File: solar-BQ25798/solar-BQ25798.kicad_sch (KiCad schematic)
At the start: 83 parts, among them J101 Power In, J102 Power OUT, J103 Power OUT, Q101 DMP4013LFGQ-13, Q102 2N7002, U101 HT75xx-1-SOT89, U102 INA219AxDCN

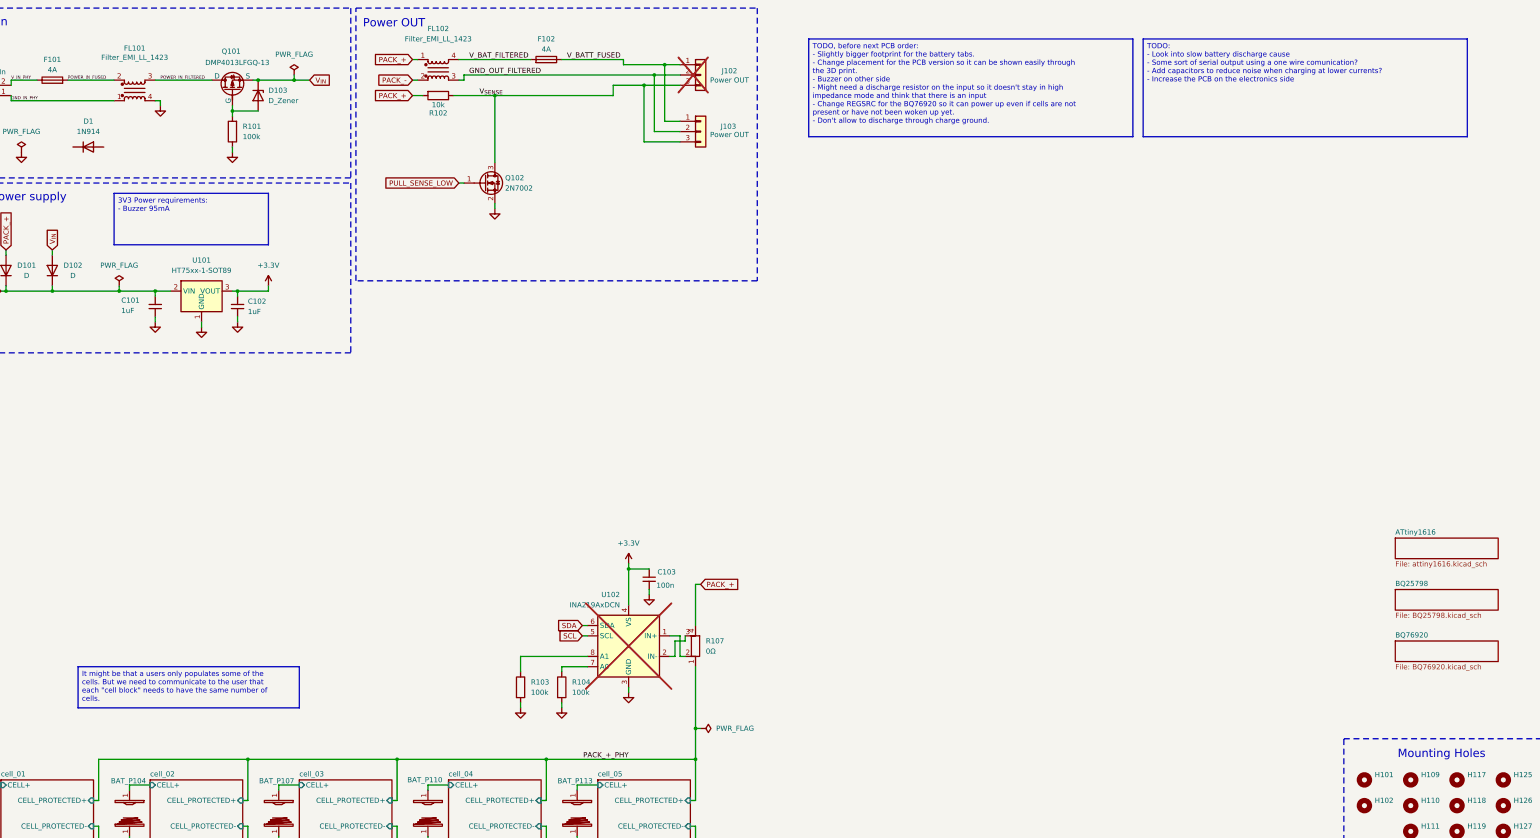
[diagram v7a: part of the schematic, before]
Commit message: Fix pin for serial out and other small fixes
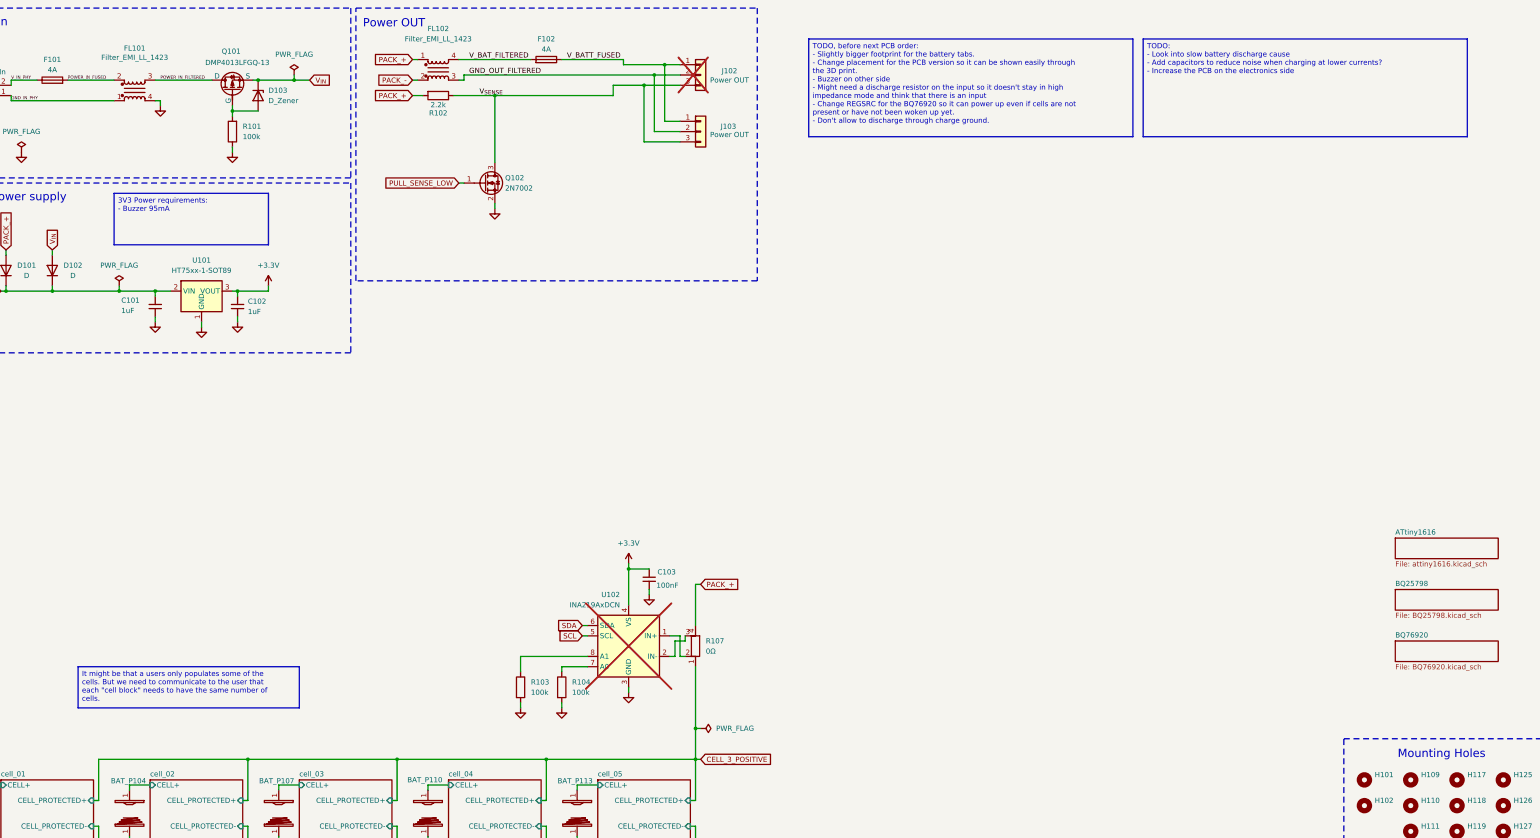
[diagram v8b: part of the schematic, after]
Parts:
- removed D1: 1N914, Diode_THT:D_DO-35_SOD27_P7.62mm_Horizontal, symbol Diode:1N914
- C103: value 100n -> 100nF; LCSC Part C307331 -> C1525
- R102: value 10k -> 2.2k; LCSC Part C25744 -> C25879
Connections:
- net PACK_+_PHY renamed CELL_3_POSITIVE
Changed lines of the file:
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@@
 		)
 	)
-	(text_box "TODO:\n- Look into slow battery discharge cause\n- Some sort of serial output using a one wire comunication?\n- Add capacitors to reduce noise when charging at lower currents?\n- Increase the PCB on the electronics side\n"
+	(text_box "TODO:\n- Look into slow battery discharge cause\n- Add capacitors to reduce noise when charging at lower currents?\n- Increase the PCB on the electronics side\n"
 		(exclude_from_sim no)
 		(at 307.34 20.32 0)
@@
 	(wire
 		(pts
+			(xy 196.85 198.12) (xy 198.12 198.12)
+		)
+		(stroke
+			(width 0)
+			(type default)
+		)
+	)
+	(wire
+		(pts
 			(xy 168.91 167.64) (xy 170.18 167.64)
 		)
@@
 		)
 	)
-	(label "PACK_+_PHY"
-		(at 180.34 198.12 180)
-		(effects
-			(font
-				(size 1.27 1.27)
-			)
-			(justify right bottom)
-		)
-	)
 	(global_label "CELL_2_POSITIVE"
 		(shape input)
@@
 		)
 	)
+	(global_label "CELL_3_POSITIVE"
+		(shape input)
+		(at 198.12 198.12 0)
+		(fields_autoplaced yes)
+		(effects
+			(font
+				(size 1.27 1.27)
+			)
+			(justify left)
+		)
+		(property "Intersheetrefs" "${INTERSHEET_REFS}"
+			(at 216.9499 198.12 0)
+			(hide yes)
+			(show_name no)
+			(do_not_autoplace no)
+			(effects
+				(font
+					(size 1.27 1.27)
+				)
+				(justify left)
+			)
+		)
+	)
 	(global_label "CELL_1_POSITIVE"
 		(shape input)
@@
 			)
 		)
-		(property "Value" "100n"
+		(property "Value" "100nF"
 			(at 187.198 155.194 0)
 			(show_name no)
@@
 			)
 		)
-		(property "LCSC Part" "C307331"
+		(property "LCSC Part" "C1525"
 			(at 185.42 153.67 0)
 			(hide yes)
@@
 			)
 		)
-		(property "Value" "10k"
+		(property "Value" "2.2k"
 			(at 133.35 36.576 90)
 			(show_name no)
@@
 			)
 		)
-		(property "LCSC Part" "C25744"
+		(property "LCSC Part" "C25879"
 			(at 133.35 34.29 90)
 			(hide yes)
@@
 					(unit 1)
 				)
-			)
-		)
-	)
-	(symbol
-		(lib_id "Diode:1N914")
-		(at 46.99 46.99 0)
-		(unit 1)
-		(body_style 1)
-		(exclude_from_sim no)
-		(in_bom yes)
-		(on_board yes)
-		(in_pos_files yes)
-		(dnp no)
-		(fields_autoplaced yes)
-		(property "Reference" "D1"
-			(at 46.99 40.64 0)
-			(show_name no)
-			(do_not_autoplace no)
-			(effects
-				(font
-					(size 1.27 1.27)
-				)
-			)
-		)
-		(property "Value" "1N914"
-			(at 46.99 43.18 0)
-			(show_name no)
-			(do_not_autoplace no)
-			(effects
-				(font
-					(size 1.27 1.27)
-				)
-			)
-		)
-		(property "Footprint" "Diode_THT:D_DO-35_SOD27_P7.62mm_Horizontal"
-			(at 46.99 51.435 0)
-			(hide yes)
-			(show_name no)
-			(do_not_autoplace no)
-			(effects
-				(font
-					(size 1.27 1.27)
-				)
-			)
-		)
-		(property "Datasheet" "http://www.vishay.com/docs/85622/1n914.pdf"
-			(at 46.99 46.99 0)
-			(hide yes)
-			(show_name no)
-			(do_not_autoplace no)
-			(effects
-				(font
-					(size 1.27 1.27)
-				)
-			)
-		)
-		(property "Description" "100V 0.3A Small Signal Fast Switching Diode, DO-35"
-			(at 46.99 46.99 0)
-			(hide yes)
-			(show_name no)
-			(do_not_autoplace no)
-			(effects
-				(font
-					(size 1.27 1.27)
-				)
-			)
-		)
-		(property "Sim.Device" "D"
-			(at 46.99 46.99 0)
-			(hide yes)
-			(show_name no)
-			(do_not_autoplace no)
-			(effects
-				(font
-					(size 1.27 1.27)
-				)
-			)
-		)
-		(property "Sim.Pins" "1=K 2=A"
-			(at 46.99 46.99 0)
-			(hide yes)
-			(show_name no)
-			(do_not_autoplace no)
-			(effects
-				(font
-					(size 1.27 1.27)
-				)
-			)
-		)
-		(pin "2"
-		)
-		(pin "1"
-		)
-		(instances
-			(project "solar-BQ25798"
-				(path "/822b745e-d66e-4222-a6d2-360780548724"
-					(reference "D1")
-					(unit 1)
-				)
